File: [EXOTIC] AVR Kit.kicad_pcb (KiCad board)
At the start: 2 copper layers, 105 x 80 mm, 56 parts, among them J1 Barrel_Jack_Switch, J2 AVR-ISP-10, J3 USB_B, J4 Port A, J5 Port B, J6 Port C + D7, J7 Port D, J8 5V Headers, J9 3.3 V Headers, Q1 AO3401A, Q2 SI2302, SW1 SW_Push, SW2 SW_DPDT_x2, U1 ATmega32A-P, U2 AMS1117-5.0, U3 AMS1117-3.3, U4 LM324, U5 LM339, U6 CH340C, Y1 16 MHz

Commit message: Minor Tweak
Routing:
- net /Power Management Circuitry/V_{In} (Unfused): track 73.5 -> 72.7 mm
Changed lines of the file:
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@@
   (segment (start 173.99 79.02) (end 173.99 80.15) (width 0.4) (layer "F.Cu") (net 87))
   (segment (start 152.4 69.85) (end 156.21 69.85) (width 0.4) (layer "F.Cu") (net 88))
-  (segment (start 148.59 64.635) (end 148.59 66.04) (width 0.4) (layer "F.Cu") (net 88))
+  (segment (start 139.7 59.69) (end 144.78 59.69) (width 0.4) (layer "F.Cu") (net 88))
+  (segment (start 119.38 66.04) (end 119.38 60.96) (width 0.4) (layer "F.Cu") (net 88))
   (segment (start 146.145 61.055) (end 146.145 62.19) (width 0.4) (layer "F.Cu") (net 88))
   (segment (start 118.11 78.74) (end 116.84 77.47) (width 0.4) (layer "F.Cu") (net 88))
-  (segment (start 144.78 59.69) (end 146.145 61.055) (width 0.4) (layer "F.Cu") (net 88))
+  (segment (start 148.59 64.635) (end 148.59 66.04) (width 0.4) (layer "F.Cu") (net 88))
+  (segment (start 119.38 60.96) (end 123.19 57.15) (width 0.4) (layer "F.Cu") (net 88))
   (segment (start 137.16 57.15) (end 139.7 59.69) (width 0.4) (layer "F.Cu") (net 88))
   (segment (start 148.59 66.04) (end 152.4 69.85) (width 0.4) (layer "F.Cu") (net 88))
-  (segment (start 119.38 66.04) (end 119.38 59.69) (width 0.4) (layer "F.Cu") (net 88))
+  (segment (start 123.19 57.15) (end 137.16 57.15) (width 0.4) (layer "F.Cu") (net 88))
   (segment (start 121.985 78.74) (end 118.11 78.74) (width 0.4) (layer "F.Cu") (net 88))
-  (segment (start 121.92 57.15) (end 137.16 57.15) (width 0.4) (layer "F.Cu") (net 88))
-  (segment (start 139.7 59.69) (end 144.78 59.69) (width 0.4) (layer "F.Cu") (net 88))
+  (segment (start 144.78 59.69) (end 146.145 61.055) (width 0.4) (layer "F.Cu") (net 88))
   (segment (start 116.84 77.47) (end 116.84 68.58) (width 0.4) (layer "F.Cu") (net 88))
-  (segment (start 119.38 59.69) (end 121.92 57.15) (width 0.4) (layer "F.Cu") (net 88))
   (segment (start 146.145 62.19) (end 148.59 64.635) (width 0.4) (layer "F.Cu") (net 88))
   (segment (start 116.84 68.58) (end 119.38 66.04) (width 0.4) (layer "F.Cu") (net 88))

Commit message: More Tweaks
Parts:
- moved R2 1.97 mm to (198.3, 57.8), turned to 0 degrees
- moved R3 1.83 mm to (201.4, 61.0), turned to 0 degrees
- moved C8 1.59 mm to (163.8, 58.2)
- moved J3 0.10 mm to (128.3, 67.3)
- moved J1 0.10 mm to (157.0, 65.9)
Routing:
- net Net-(U4A--): track 16.2 -> 11.7 mm
- net +5V_{OCP}: track 104.0 -> 102.7 mm
- net Net-(U4D--): track 10.3 -> 11.4 mm

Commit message: Pre Rev. 4
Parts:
- removed Q2: SI2302, Package_TO_SOT_SMD:SOT-23_Handsoldering
- removed the R10 at (174.0, 77.5)
- removed R5: 10 kΩ, Resistor_SMD:R_1206_3216Metric_Pad1.30x1.75mm_HandSolder
- removed R7, R8: 0.22 Ω, Resistor_THT:R_Axial_DIN0614_L14.3mm_D5.7mm_P7.62mm_Vertical
- removed R9: 0 Ω, Resistor_SMD:R_1206_3216Metric_Pad1.30x1.75mm_HandSolder
- removed RV1, RV2, RV3: 10 kΩ, Potentiometer_THT:Potentiometer_Bourns_3296W_Vertical
- removed U5: LM339, Package_SO:SOIC-14_3.9x8.7mm_P1.27mm
- added F2: Polyfuse_Small, Capacitor_THT:C_Disc_D10.5mm_W5.0mm_P5.00mm, F.Cu at (172.7, 83.9)
- R2: value 10 kΩ -> 0 Ω
- R3: value 330 kΩ -> 0 Ω
- moved G*** 86.7 mm to (207.0, 118.7), turned to -90 degrees
- moved U4 82.6 mm to (120.7, 85.1)
- moved R2 74.4 mm to (125.7, 74.3), turned to 180 degrees
- moved R3 69.9 mm to (132.7, 74.3), turned to 180 degrees
- moved J9 64.8 mm to (148.6, 67.3), turned to 90 degrees
- moved SW2 57.3 mm to (199.4, 74.9)
- moved J1 51.5 mm to (207.6, 74.9), turned to 0 degrees
- moved J8 50.3 mm to (161.9, 67.3), turned to 90 degrees
- moved G*** 36.2 mm to (207.0, 87.6)
- moved C7 35.7 mm to (143.5, 72.7), turned to -90 degrees
- moved U3 30.6 mm to (148.6, 74.3), turned to 90 degrees
- moved H1 26.9 mm to (142.0, 67.0)
- moved F1 22.2 mm to (179.7, 74.9), turned to 180 degrees
- moved C5 19.3 mm to (153.7, 74.3)
- moved C8 17.6 mm to (156.8, 74.3)
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- renumbered R11 to R10
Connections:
- C8 pad 1: +5V_{OCP} -> +5V
- F1 pad 1: Net-(SW2B-B) -> Net-(SW2A-B)
- J1 pad 1: /Power Management Circuitry/V_{In} (Unfused) -> Net-(SW2A-C)
- J8 pad 1: +5V_{OCP} -> +5V
- J8 pad 2: +5V_{OCP} -> +5V
- R1 pad 1: +5V -> +5V_{PPTC}
- R10 pad 1: +5V -> +5V_{PPTC}
- R2 pad 1: -V_{In} -> Net-(R2-Pad1)
- R2 pad 2: Net-(U4A--) -> Net-(U4C--)
- R3 pad 1: Net-(U4A--) -> +3V3
- R3 pad 2: Net-(U4D--) -> Net-(R2-Pad1)
- R4 pad 2: /Power Management Circuitry/V_{In} (Unfused) -> +V_{In}
- SW2 pad 2: unconnected-(SW2A-B-Pad2) -> Net-(SW2A-B)
- SW2 pad 3: unconnected-(SW2A-C-Pad3) -> Net-(SW2A-C)
- SW2 pad 5: Net-(SW2B-B) -> unconnected-(SW2B-B-Pad5)
- SW2 pad 6: /Power Management Circuitry/V_{In} (Unfused) -> unconnected-(SW2B-C-Pad6)
- U1 pad 10: +5V -> +5V_{PPTC}
- U2 pad 2: +5V_{OCP} -> +5V
- U4 pad 1: Net-(U4D--) -> (no net)
- U4 pad 10: unconnected-(U4C-+-Pad10) -> +V_{In}
- U4 pad 11: -V_{In} -> GND
- U4 pad 12: Net-(U4D-+) -> (no net)
- U4 pad 13: Net-(U4D--) -> (no net)
- U4 pad 14: Net-(Q2-G) -> (no net)
- U4 pad 2: Net-(U4A--) -> (no net)
- U4 pad 3: Net-(U4A-+) -> (no net)
- U4 pad 4: +V_{In} -> +5V
- U4 pad 5: Net-(U4B-+) -> (no net)
- U4 pad 6: Net-(U4B--) -> (no net)
- U4 pad 7: Net-(U4A-+) -> (no net)
- U4 pad 8: unconnected-(U4-Pad8) -> Net-(Q1-G)
- U4 pad 9: unconnected-(U4C---Pad9) -> Net-(U4C--)
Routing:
- net +5V_{OCP}: track 102.7 -> 0.00 mm
- net /MOSI: track 72.6 -> 172.9 mm
- net +5V: track 207.5 -> 134.3 mm, vias 2 -> 0
- net /Power Management Circuitry/V_{In} (Unfused): track 72.6 -> 0.00 mm
- net +5V_{PPTC}: track 0.00 -> 49.3 mm
- net Net-(U5A--): track 48.3 -> 0.00 mm
- net Net-(R10-Pad1): track 37.5 -> 0.00 mm
- net -V_{In}: track 123.4 -> 87.4 mm
- net +3V3: track 53.4 -> 29.2 mm
- net Net-(U4A-+): track 18.4 -> 0.00 mm
- net Net-(U4C--): track 0.00 -> 16.4 mm
- net /~{RESET}: track 232.7 -> 218.1 mm
- net /MISO: track 158.8 -> 173.1 mm
- net Net-(Q2-G): track 14.1 -> 0.00 mm
- net Net-(SW2B-B): track 13.8 -> 0.00 mm
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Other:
- board size 105 x 80 mm -> 105 x 75 mm

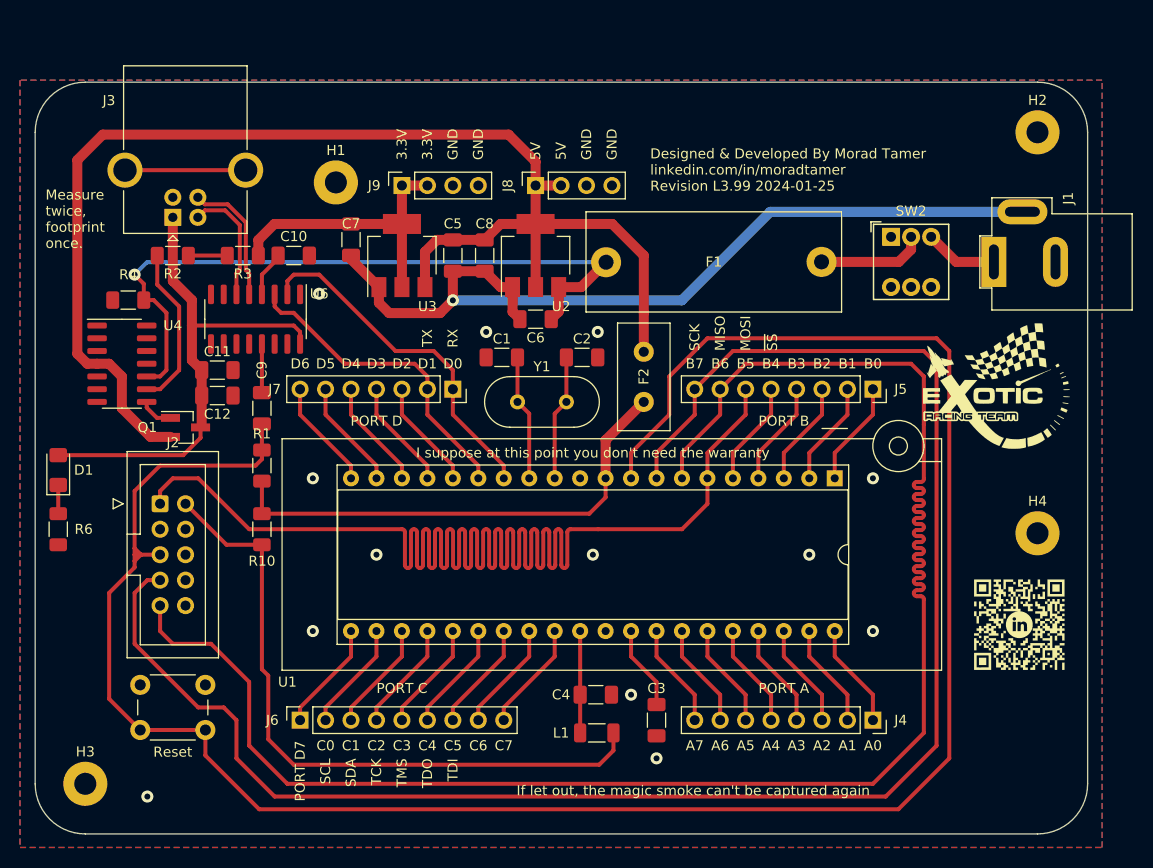
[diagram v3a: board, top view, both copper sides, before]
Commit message: Migrated from KiCAD 7.0 to 8.0
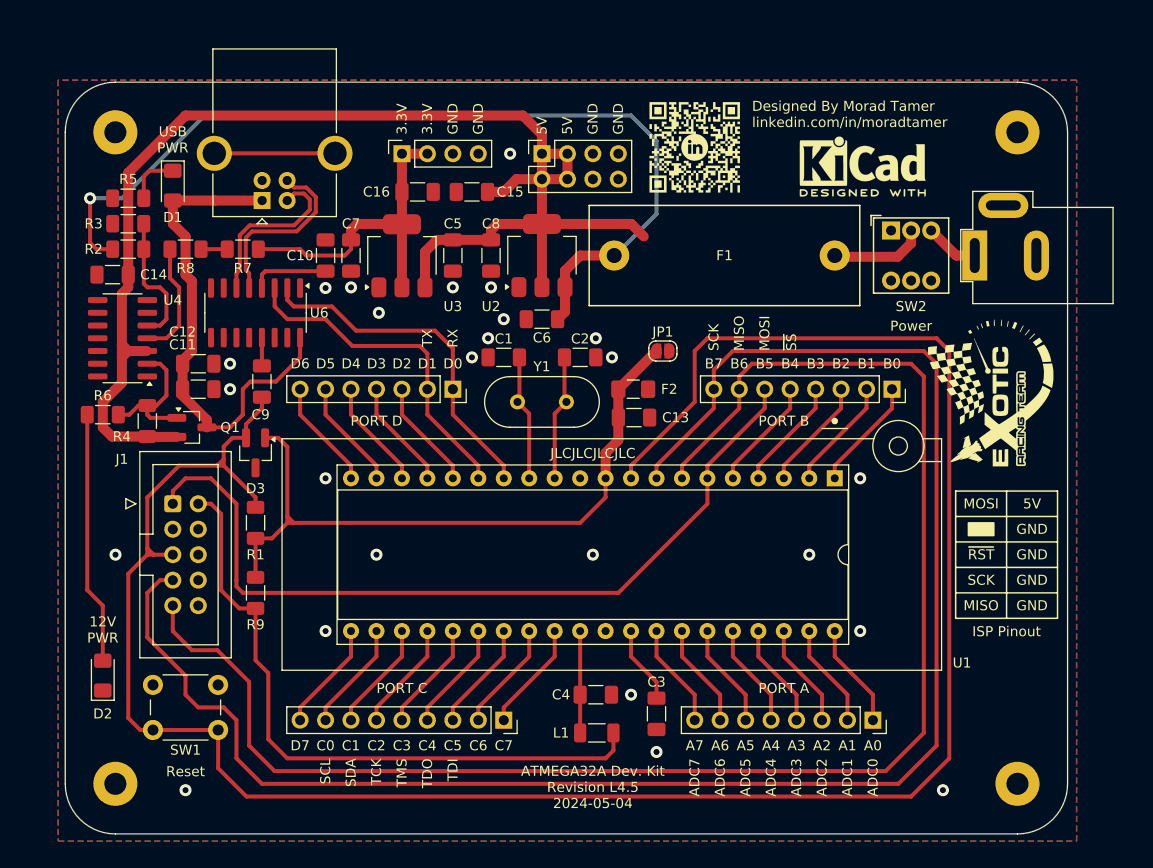
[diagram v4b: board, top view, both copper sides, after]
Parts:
- removed J8: 5V Headers, Connector_PinSocket_2.54mm:PinSocket_1x04_P2.54mm_Vertical
- added C13: 100 nF, Capacitor_SMD:C_1206_3216Metric_Pad1.33x1.80mm_HandSolder, F.Cu at (171.7, 90.5)
- added C14: 100 nF, Capacitor_SMD:C_1206_3216Metric_Pad1.33x1.80mm_HandSolder, F.Cu at (119.7, 76.2)
- added C15: 100 nF, Capacitor_SMD:C_1206_3216Metric_Pad1.33x1.80mm_HandSolder, F.Cu at (155.6, 67.9)
- added C16: 100 nF, Capacitor_SMD:C_1206_3216Metric_Pad1.33x1.80mm_HandSolder, F.Cu at (150.2, 67.9)
- added D2: LED, LED_SMD:LED_1206_3216Metric_Pad1.42x1.75mm_HandSolder, F.Cu at (118.7, 116.2)
- added D3: BAS16, Package_TO_SOT_SMD:SOT-23_Handsoldering, F.Cu at (134.0, 94.0)
- added J10: 5 V Headers, Connector_PinSocket_2.54mm:PinSocket_2x04_P2.54mm_Vertical, F.Cu at (162.6, 64.1)
- added JP1: PPTC Bypass, Jumper:SolderJumper-2_P1.3mm_Open_RoundedPad1.0x1.5mm, F.Cu at (174.6, 83.8)
- added R2: 10 kΩ, Resistor_SMD:R_1206_3216Metric_Pad1.30x1.75mm_HandSolder, F.Cu at (121.3, 73.7)
- added R4: 470 Ω, Resistor_SMD:R_1206_3216Metric_Pad1.30x1.75mm_HandSolder, F.Cu at (123.2, 90.8)
- added R6: 10 kΩ, Resistor_SMD:R_1206_3216Metric_Pad1.30x1.75mm_HandSolder, F.Cu at (118.7, 90.2)
- added REF**: KiCad-Logo2_5mm_SilkScreen, Symbol:KiCad-Logo2_5mm_SilkScreen, F.Cu at (194.6, 65.4)
- F2: footprint Capacitor_THT:C_Disc_D10.5mm_W5.0mm_P5.00mm -> Fuse:Fuse_1206_3216Metric_Pad1.42x1.75mm_HandSolder
- R5: renamed from R6; value 1 kΩ -> 10 kΩ
- U4: value LM324 -> LM339; footprint Package_SO:SO-14_3.9x8.65mm_P1.27mm -> Package_SO:SOIC-14_3.9x8.7mm_P1.27mm
- moved G*** 57.6 mm to (177.8, 63.5)
- moved R5 33.8 mm to (121.3, 68.6), turned to 180 degrees
- moved D1 30.6 mm to (125.7, 67.3), turned to -90 degrees
- moved H4 25.1 mm to (210.0, 127.0)
- moved H1 22.6 mm to (120.0, 62.0)
- moved J6 20.3 mm to (158.8, 120.7), turned to -90 degrees
- moved G*** 15.3 mm to (203.8, 103.8), turned to 180 degrees
- moved J3 9.07 mm to (134.6, 68.8)
- moved R3 7.62 mm to (121.3, 71.1)
- moved R9 6.38 mm to (134.0, 108.0)
- moved R1 5.75 mm to (134.0, 101.0)
- moved F2 3.88 mm to (171.7, 87.6), turned to 180 degrees
- moved C12 3.70 mm to (128.3, 85.1)
- moved C10 3.18 mm to (141.0, 74.3), turned to -90 degrees
- moved J9 3.17 mm to (148.6, 64.1)
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- renumbered J2 to J1, J1 to J2, R4 to R3, R3 to R7, R2 to R8, R10 to R9
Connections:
- C5 pad 2: -V_{In} -> GND
- C6 pad 2: -V_{In} -> GND
- C7 pad 2: -V_{In} -> GND
- C8 pad 2: -V_{In} -> GND
- F1 pad 1: Net-(SW2A-B) -> +V_{In}
- F1 pad 2: +V_{In} -> Net-(SW2A-B)
- J2 pad 2: -V_{In} -> GND
- J6 pad 1: /PD7 -> /PC7
- J6 pad 2: /SCL -> /PC6
- J6 pad 3: /SDA -> /TDI
- J6 pad 4: /TCK -> /TDO
- J6 pad 6: /TDO -> /TCK
- J6 pad 7: /TDI -> /SDA
- J6 pad 8: /PC6 -> /SCL
- J6 pad 9: /PC7 -> /PD7
- Q1 pad 1: Net-(Q1-G) -> /Power Management Circuitry/Comparator
- R3 pad 2: +V_{In} -> Net-(U4A-+)
- R8 pad 2: Net-(U4C--) -> Net-(U4A--)
- U2 pad 1: -V_{In} -> GND
- U3 pad 1: -V_{In} -> GND
- U4 pad 1: (no net) -> unconnected-(U4-Pad1)
- U4 pad 10: +V_{In} -> unconnected-(U4C---Pad10)
- U4 pad 11: GND -> unconnected-(U4C-+-Pad11)
- U4 pad 12: (no net) -> GND
- U4 pad 13: (no net) -> unconnected-(U4-Pad13)
- U4 pad 14: (no net) -> unconnected-(U4-Pad14)
- U4 pad 2: (no net) -> /Power Management Circuitry/Comparator
- U4 pad 3: (no net) -> +5V
- U4 pad 4: +5V -> Net-(U4A--)
- U4 pad 5: (no net) -> Net-(U4A-+)
- U4 pad 6: (no net) -> unconnected-(U4B---Pad6)
- U4 pad 7: (no net) -> unconnected-(U4B-+-Pad7)
- U4 pad 8: Net-(Q1-G) -> unconnected-(U4D---Pad8)
- U4 pad 9: Net-(U4C--) -> unconnected-(U4D-+-Pad9)
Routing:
- net /MOSI: track 172.9 -> 82.2 mm
- net -V_{In}: track 87.4 -> 0.00 mm, vias 1 -> 0
- net Net-(D2-A): track 0.00 -> 25.2 mm
- net +V_{In}: track 70.5 -> 92.0 mm
- net +5V_{PPTC}: track 49.3 -> 68.3 mm
- net /MISO: track 173.1 -> 156.1 mm
- net Net-(U4C--): track 16.4 -> 0.00 mm
- net /Power Management Circuitry/Comparator: track 0.00 -> 14.3 mm
- net Net-(U4A-+): track 0.00 -> 13.4 mm
- net Net-(U4A--): track 0.00 -> 11.7 mm
- net /USB_D+: track 13.1 -> 18.3 mm
- net /USB_D-: track 12.1 -> 17.3 mm
- net +5V: track 134.3 -> 138.7 mm
- net /~{RESET}: track 218.1 -> 222.1 mm
- net +3V3: track 29.2 -> 32.9 mm
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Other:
- board size 105 x 75 mm -> 100 x 75 mm
- board text added: "12V PWR"
- board text added: "ADC0"
- board text added: "ADC1"
- board text added: "ADC2"
- board text added: "ADC3"
- board text added: "ADC4"
- board text added: "ADC5"
- board text added: "ADC6"
- board text added: "ADC7"
- board text added: "ATMEGA32A Dev. Kit Revision ${REVISION} ${ISSUE_DATE}"
- board text added: "D7"
- board text added: "Designed By Morad Tamer linkedin.com/in/moradtamer"
- board text added: "ISP Pinout"
- board text added: "JLCJLCJLCJLC"
- board text added: "Power"
- board text added: "Reset"
- board text added: "USB PWR"
- board text added: "~{RST}"
- board text removed: "Designed & Developed By Morad Tamer linkedin.com/in/moradtamer Revision ${REVISION} ${ISSUE_DATE}"
- board text removed: "PORT D7"

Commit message: Updated Images
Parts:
- moved F2 1.69 mm to (173.4, 87.6)
- moved JP1 1.42 mm to (173.4, 83.2)
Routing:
- net +5V: track 138.7 -> 155.2 mm
- net +5V_{PPTC}: track 68.3 -> 69.0 mm
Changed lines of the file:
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@@
 		)
 		(property "Value" "100 nF"
-			(at 4.445 0 360)
+			(at 4.445 0 0)
 			(layer "F.Fab")
 			(effects
@@
 		)
 		(fp_text user "${REFERENCE}"
-			(at 0 0 360)
+			(at 0 0 0)
 			(layer "F.Fab")
 			(effects
@@
 	(footprint "Jumper:SolderJumper-2_P1.3mm_Open_RoundedPad1.0x1.5mm"
 		(layer "F.Cu")
-		(at 174.625 83.82 180)
+		(at 173.355 83.185 180)
 		(descr "SMD Solder Jumper, 1x1.5mm, rounded Pads, 0.3mm gap, open")
 		(tags "solder jumper open")
@@
 	(footprint "Fuse:Fuse_1206_3216Metric_Pad1.42x1.75mm_HandSolder"
 		(layer "F.Cu")
-		(at 171.6675 87.63 180)
+		(at 173.355 87.63 180)
 		(descr "Fuse SMD 1206 (3216 Metric), square (rectangular) end terminal, IPC_7351 nominal with elongated pad for handsoldering. (Body size source: http://www.tortai-tech.com/upload/download/2011102023233369053.pdf), generated with kicad-footprint-generator")
 		(tags "fuse handsolder")
 		(property "Reference" "F2"
-			(at -3.5925 0 0)
+			(at 0 1.905 0)
 			(layer "F.SilkS")
 			(effects
@@
 		)
 		(property "Local Seller" "https://makerselectronics.com/product/resettable-fuse-lvr016k-240v-160ma-2a-through-hole"
-			(at 0 0 270)
+			(at 0 0 -90)
 			(layer "F.Fab")
 			(hide yes)
@@
 	)
 	(segment
-		(start 162.56 71.145)
-		(end 171.475 71.145)
+		(start 119.66 92.355)
+		(end 123.19 92.355)
 		(width 1)
 		(layer "F.Cu")
@@
 	)
 	(segment
-		(start 119.66 92.355)
-		(end 123.19 92.355)
+		(start 174.8425 87.63)
+		(end 174.8425 84.0225)
 		(width 1)
 		(layer "F.Cu")
@@
 	)
 	(segment
-		(start 121.285 83.82)
-		(end 120.65 84.455)
+		(start 172.11 71.145)
+		(end 162.56 71.145)
 		(width 1)
 		(layer "F.Cu")
@@
 	)
 	(segment
-		(start 171.475 71.145)
-		(end 172.72 72.39)
+		(start 121.285 83.82)
+		(end 120.65 84.455)
 		(width 1)
 		(layer "F.Cu")
@@
 	)
 	(segment
+		(start 174.8425 84.0225)
+		(end 174.005 83.185)
+		(width 1)
+		(layer "F.Cu")
+		(net 14)
+	)
+	(segment
 		(start 121.285 77.47)
 		(end 120.65 78.105)
@@
 	)
 	(segment
+		(start 174.005 83.185)
+		(end 174.005 73.04)
+		(width 1)
+		(layer "F.Cu")
+		(net 14)
+	)
+	(segment
 		(start 120.65 83.185)
 		(end 121.285 83.82)
@@
 	)
 	(segment
+		(start 174.005 73.04)
+		(end 172.11 71.145)
+		(width 1)
+		(layer "F.Cu")
+		(net 14)
+	)
+	(segment
 		(start 162.56 66.675)
 		(end 162.56 71.145)
@@
 	)
 	(segment
+		(start 171.8675 84.0225)
+		(end 171.8675 87.63)
+		(width 1)
+		(layer "F.Cu")
+		(net 51)
+	)
+	(segment
 		(start 136.25 92.48)
 		(end 134.935 92.48)
@@
 	)
 	(segment
-		(start 168.91 93.98)
-		(end 168.91 96.52)
+		(start 172.705 83.185)
+		(end 171.8675 84.0225)
 		(width 1)
 		(layer "F.Cu")
@@
 	)
 	(segment
-		(start 170.18 87.63)
-		(end 170.18 87.615)
+		(start 168.91 93.98)
+		(end 168.91 96.52)
 		(width 1)
 		(layer "F.Cu")
@@
 	)
 	(segment
-		(start 137.16 100.965)
-		(end 137.16 100.33)
-		(width 0.4)
+		(start 171.8675 87.63)
+		(end 170.815 87.63)
+		(width 1)
 		(layer "F.Cu")
 		(net 51)
 	)
 	(segment
-		(start 170.18 87.63)
-		(end 170.18 90.4625)
-		(width 1)
+		(start 137.16 100.965)
+		(end 137.16 100.33)
+		(width 0.4)
 		(layer "F.Cu")
 		(net 51)
@@
 	)
 	(segment
+		(start 170.18 88.265)
+		(end 170.18 90.4625)
+		(width 1)
+		(layer "F.Cu")
+		(net 51)
+	)
+	(segment
 		(start 137.16 100.33)
 		(end 137.795 100.965)
@@
 	)
 	(segment
-		(start 170.18 87.615)
-		(end 173.975 83.82)
+		(start 170.815 87.63)
+		(end 170.18 88.265)
 		(width 1)
 		(layer "F.Cu")
